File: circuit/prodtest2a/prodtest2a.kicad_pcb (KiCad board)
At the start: 2 copper layers, 191.5 x 166.3 mm, 121 parts, among them J1 Conn_02x05_Odd_Even, J10 Banana Black, J2 Conn_02x20_Odd_Even, J3 Conn_02x05_Odd_Even, J4 Conn_01x05, J5 Conn_01x05, J6 Conn_Coaxial, J7 Conn_01x03, J8 Barrel_Jack, J9 Banana Red, K1 HE721A, K10 HE721A, K11 HE721A, K12 HE721A, K13 HE721A, K14 HE721A, K15 HE721A, K16 HE721A, K17 HE721A, K18 HE721A, K19 HE721A, K2 HE721A, K20 HE721A, K21 HE721A, K22 HE721A, K23 HE721A, K24 HE721A, K25 HE721A, K26 HE721A, K27 HE721A, K28 HE721A, K3 HE721A, K4 HE721A, K5 HE721A, K6 HE721A, K7 HE721A, K8 HE721A, K9 HE721A, Q1 IPP034N03L, U1 MCP601-xP, U10 ULN2003A, U11 ULN2003A, U2 LM1084-ADJ, U3 74HCT04, U4 74HCT04, U5 74HCT04, U6 74HCT04, U7 74HCT04, U8 ULN2003A, U9 ULN2003A

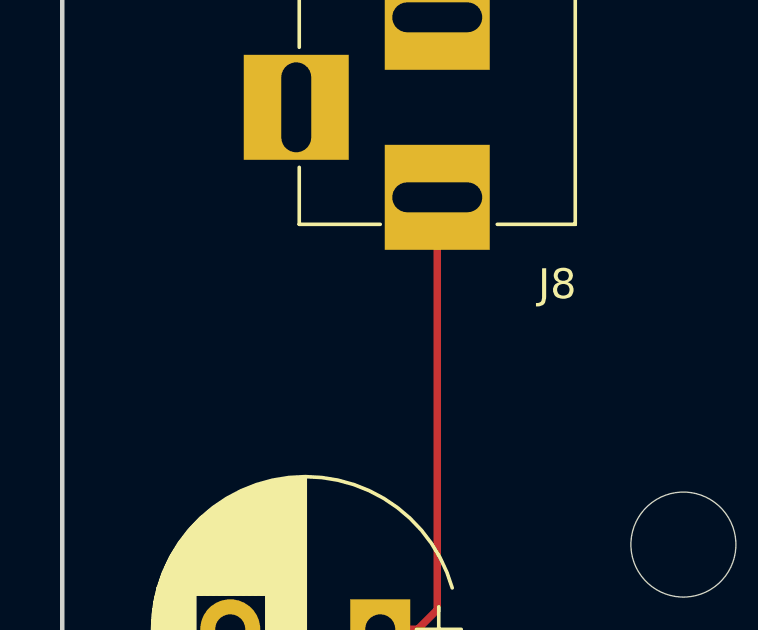
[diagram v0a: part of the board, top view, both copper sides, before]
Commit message: prodtest2a: Mark voltage of power input
Signed-off-by: Gavan Fantom <gavan.fantom@unipart.io>
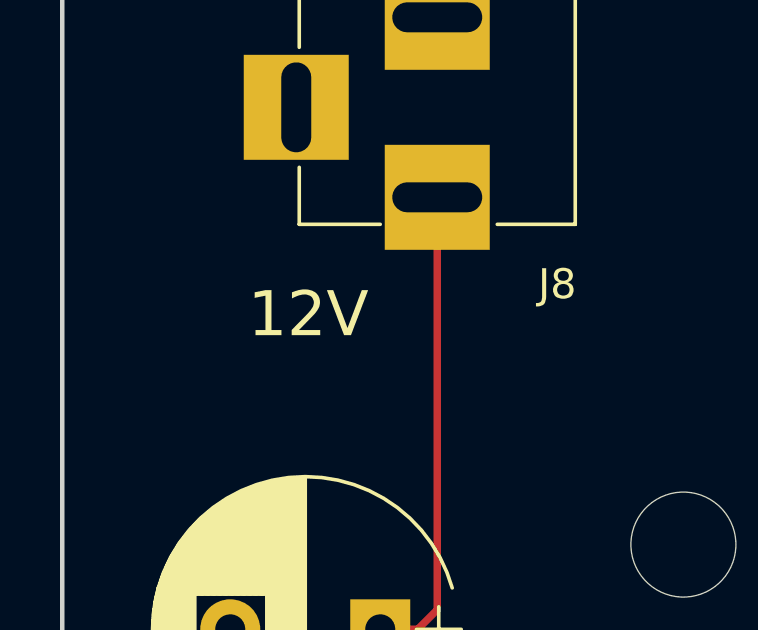
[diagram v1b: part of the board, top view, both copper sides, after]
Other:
- board text added: "12V"
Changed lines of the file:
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@@
     (links 416)
     (no_connects 0)
-    (area 12.924999 20.924999 204.555001 187.375001)
+    (area 9.639999 -3.025 207.840001 194.449882)
     (thickness 1.6)
-    (drawings 57)
+    (drawings 58)
     (tracks 3630)
     (zones 0)
@@
     (pad 1 np_thru_hole circle (at 0 0 90) (size 3.5 3.5) (drill 3.5) (layers *.Cu *.Mask))
   )
+  (gr_text 12V (at 21.2 36.4) (layer F.SilkS)
+    (effects (font (size 1.5 1.5) (thickness 0.3)))
+  )
   (gr_text "Tail tag v2a/b\nProduction tester\nVersion 1" (at 139.6 62) (layer F.SilkS)
